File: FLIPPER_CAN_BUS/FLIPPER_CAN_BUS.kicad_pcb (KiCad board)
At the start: 2 copper layers, 62.8 x 21.2 mm, 25 parts, among them J1 Conn_01x02, J2 Conn_01x10_Socket, J3 Conn_01x08_Socket, U1 TJA1051T/3, U2 MCP2515-xST, U3 AP3602AKTR-G1, Y1 16 Mhz

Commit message: upd
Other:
- board text added: "+3V3"
- board text added: "5V"
- board text added: "CS"
- board text added: "GND"
- board text added: "INT"
- board text added: "MISO"
- board text added: "MOSI"
- board text added: "RST"
- board text added: "SCK"
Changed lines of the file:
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@@
     (property "manf#" "0603F104Z160CT")
     (attr smd)
-    (fp_text reference "C11" (at 2.130777 0.011726 -180) (layer "F.SilkS")
+    (fp_text reference "C11" (at -0.042823 -1.190674 -90) (layer "F.SilkS")
         (effects (font (size 0.5 0.5) (thickness 0.125)))
     )
@@
     (property "manf#" "0805YC106KAT2A")
     (attr smd)
-    (fp_text reference "C8" (at 2.133277 0.091726 -180) (layer "F.SilkS")
+    (fp_text reference "C8" (at 0.000477 1.110126 -90) (layer "F.SilkS")
         (effects (font (size 0.5 0.5) (thickness 0.125)))
     )
@@
   (gr_arc (start 143.8 71.6) (mid 145.497056 72.302944) (end 146.2 74)
     (stroke (width 0.1) (type default)) (layer "Edge.Cuts"))
-  (gr_text "CAN_BUS\n" (at 92.58 86.8) (layer "F.SilkS")
+  (gr_text "GND\n" (at 127.2032 88.9 90) (layer "F.SilkS")
+    (effects (font (size 0.7 0.7) (thickness 0.15)) (justify left bottom))
+  )
+  (gr_text "GND\n" (at 145.0848 88.9 90) (layer "F.SilkS")
+    (effects (font (size 0.7 0.7) (thickness 0.15)) (justify left bottom))
+  )
+  (gr_text "MISO" (at 91.6432 88.9 90) (layer "F.SilkS")
+    (effects (font (size 0.7 0.7) (thickness 0.15)) (justify left bottom))
+  )
+  (gr_text "CAN_BUS\n" (at 92.58 85.4456) (layer "F.SilkS")
     (effects (font (size 1 1) (thickness 0.25) bold) (justify left bottom))
   )
-  (gr_text "FLIPPER_SHIELD\n" (at 90.24 84.3) (layer "F.SilkS")
+  (gr_text "RST" (at 101.8032 88.9 90) (layer "F.SilkS")
+    (effects (font (size 0.7 0.7) (thickness 0.15)) (justify left bottom))
+  )
+  (gr_text "SCK" (at 96.7232 88.9 90) (layer "F.SilkS")
+    (effects (font (size 0.7 0.7) (thickness 0.15)) (justify left bottom))
+  )
+  (gr_text "FLIPPER_SHIELD\n" (at 90.24 83.6168) (layer "F.SilkS")
     (effects (font (size 1 1) (thickness 0.25) bold) (justify left bottom))
   )
+  (gr_text "5V\n" (at 86.36 88.9 90) (layer "F.SilkS")
+    (effects (font (size 0.7 0.7) (thickness 0.15)) (justify left bottom))
+  )
+  (gr_text "+3V3\n\n" (at 120.65 92.0496 90) (layer "F.SilkS")
+    (effects (font (size 0.7 0.7) (thickness 0.15)) (justify left bottom))
+  )
+  (gr_text "CS" (at 94.1324 88.9 90) (layer "F.SilkS")
+    (effects (font (size 0.7 0.7) (thickness 0.15)) (justify left bottom))
+  )
+  (gr_text "MOSI\n" (at 89.1032 88.8492 90) (layer "F.SilkS")
+    (effects (font (size 0.7 0.7) (thickness 0.15)) (justify left bottom))
+  )
+  (gr_text "GND" (at 106.3244 91.5924 90) (layer "F.SilkS")
+    (effects (font (size 0.7 0.7) (thickness 0.15)) (justify left bottom))
+  )
+  (gr_text "INT" (at 124.7648 88.9 90) (layer "F.SilkS")
+    (effects (font (size 0.7 0.7) (thickness 0.15)) (justify left bottom))
+  )
   (dimension (type aligned) (layer "Margin")

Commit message: upd
CSV
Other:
- board size 62.8 x 21.2 mm -> 62.8 x 23.2 mm
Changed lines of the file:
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@@
     (property "manf#" "PZ2.54-1*20-WZ")
     (attr through_hole)
-    (fp_text reference "J3" (at 4.385 2.27 90) (layer "B.SilkS")
+    (fp_text reference "J3" (at -1.964 -8.7736 -180) (layer "B.SilkS")
         (effects (font (size 0.5 0.5) (thickness 0.125)) (justify mirror))
     )
@@
     (property "manf#" "PZ2.54-1*20-WZ")
     (attr through_hole)
-    (fp_text reference "J2" (at 4.385 2.27 90) (layer "B.SilkS")
+    (fp_text reference "J2" (at -2.218 -12.482 -180) (layer "B.SilkS")
         (effects (font (size 0.5 0.5) (thickness 0.125)) (justify mirror))
     )
@@
   (gr_line (start 146.2 74) (end 146.2 90.4)
     (stroke (width 0.1) (type default)) (layer "Edge.Cuts"))
-  (gr_line (start 143.8 92.8) (end 86 92.8)
+  (gr_line (start 146.2 90.4) (end 146.2 92.6)
+    (stroke (width 0.1) (type default)) (layer "Edge.Cuts"))
+  (gr_arc (start 85.6 94.809943) (mid 84.037334 94.162666) (end 83.390057 92.6)
     (stroke (width 0.1) (type default)) (layer "Edge.Cuts"))
   (gr_line (start 86.2 71.592867) (end 143.8 71.592867)
     (stroke (width 0.1) (type default)) (layer "Edge.Cuts"))
-  (gr_arc (start 86 92.80768) (mid 84.156092 92.043908) (end 83.39232 90.2)
+  (gr_line (start 83.39232 90.2) (end 83.39232 92.6)
     (stroke (width 0.1) (type default)) (layer "Edge.Cuts"))
   (gr_line (start 83.39232 90.2) (end 83.39232 74.4)
     (stroke (width 0.1) (type default)) (layer "Edge.Cuts"))
-  (gr_arc (start 146.2 90.4) (mid 145.497056 92.097056) (end 143.8 92.8)
-    (stroke (width 0.1) (type default)) (layer "Edge.Cuts"))
   (gr_arc (start 83.392867 74.4) (mid 84.215057 72.415057) (end 86.2 71.592867)
+    (stroke (width 0.1) (type default)) (layer "Edge.Cuts"))
+  (gr_arc (start 146.2 92.6) (mid 145.555635 94.155635) (end 144 94.8)
+    (stroke (width 0.1) (type default)) (layer "Edge.Cuts"))
+  (gr_line (start 85.6 94.809943) (end 144 94.809943)
     (stroke (width 0.1) (type default)) (layer "Edge.Cuts"))
   (gr_arc (start 143.8 71.6) (mid 145.497056 72.302944) (end 146.2 74)
@@
   )
   (dimension (type aligned) (layer "Margin")
+    (pts (xy 85.6 94.809943) (xy 85.6 71.592867))
+    (height -5.082)
+    (gr_text "23.2171 mm" (at 79.368 83.201405 90) (layer "Margin")
+      (effects (font (size 1 1) (thickness 0.15)))
+    )
+    (format (prefix "") (suffix "") (units 3) (units_format 1) (precision 4))
+    (style (thickness 0.15) (arrow_length 1.27) (text_position_mode 0) (extension_height 0.58642) (extension_offset 0.5) keep_text_aligned)
+  )
+  (dimension (type aligned) (layer "Margin")
     (pts (xy 83.392867 74.4) (xy 146.2 74.4))
     (height -5.04)
     (gr_text "62.8071 mm" (at 114.796434 68.21) (layer "Margin")
-      (effects (font (size 1 1) (thickness 0.15)))
-    )
-    (format (prefix "") (suffix "") (units 3) (units_format 1) (precision 4))
-    (style (thickness 0.15) (arrow_length 1.27) (text_position_mode 0) (extension_height 0.58642) (extension_offset 0.5) keep_text_aligned)
-  )
-  (dimension (type aligned) (layer "Margin")
-    (pts (xy 86.2 71.592867) (xy 86.2 92.80768))
-    (height 4.289999)
-    (gr_text "21.2148 mm" (at 80.760001 82.200274 90) (layer "Margin")
       (effects (font (size 1 1) (thickness 0.15)))
     )
@@
       (pts
         (xy 83.38 71.59)
-        (xy 83.3937 92.797253)
-        (xy 146.224173 92.819707)
+        (xy 83.39491 94.669033)
+        (xy 146.225242 94.691486)
         (xy 146.212054 71.59)
       )

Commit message: upd
upd bom
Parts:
- added kibuzzard-644AD570: G***, kibuzzard-644AD570, F.Cu at (91.1, 87.8)
- added kibuzzard-644AD57B: G***, kibuzzard-644AD57B, F.Cu at (88.6, 87.8)
- added kibuzzard-644AD586: G***, kibuzzard-644AD586, F.Cu at (93.7, 88.2)
- added kibuzzard-644AD591: G***, kibuzzard-644AD591, F.Cu at (96.3, 88.0)
- added kibuzzard-644AD5B8: G***, kibuzzard-644AD5B8, F.Cu at (101.3, 88.0)
- added kibuzzard-644AD5D8: G***, kibuzzard-644AD5D8, F.Cu at (119.1, 90.6)
- added kibuzzard-644AD5FD: G***, kibuzzard-644AD5FD, F.Cu at (126.7, 88.0)
- added kibuzzard-644AD5FD: G***, kibuzzard-644AD5FD, F.Cu at (144.5, 88.0)
- added kibuzzard-644AD5FD: G***, kibuzzard-644AD5FD, F.Cu at (106.1, 90.6)
- added kibuzzard-644AD616: G***, kibuzzard-644AD616, F.Cu at (124.2, 88.0)
- D1: footprint PESD1CAN:SOT23-3 -> Package_TO_SOT_SMD:SOT-323_SC-70
- U1: footprint TJA1051T_3:SOT96-1 -> Package_SO:SOIC-8_3.9x4.9mm_P1.27mm
- U3: footprint footprints:SOT-23-6_DIO -> Package_TO_SOT_SMD:TSOT-23-6
- turned D1 to 180 degrees
- turned U1 to 0 degrees
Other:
- board text removed: "+3V3"
- board text removed: "5V"
- board text removed: "CS"
- board text removed: "GND"
- board text removed: "INT"
- board text removed: "MISO"
- board text removed: "MOSI"
- board text removed: "RST"
- board text removed: "SCK"

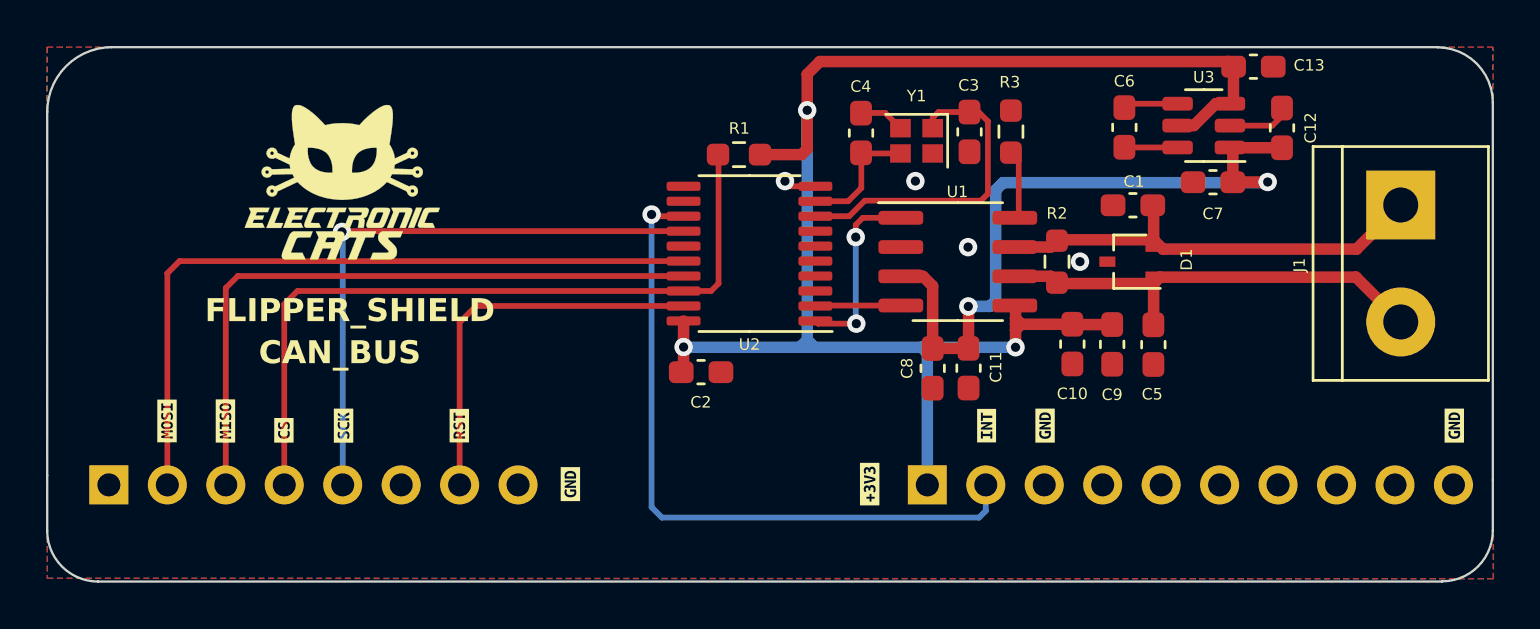
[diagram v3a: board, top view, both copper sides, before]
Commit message: Change_Capacitor_BOM
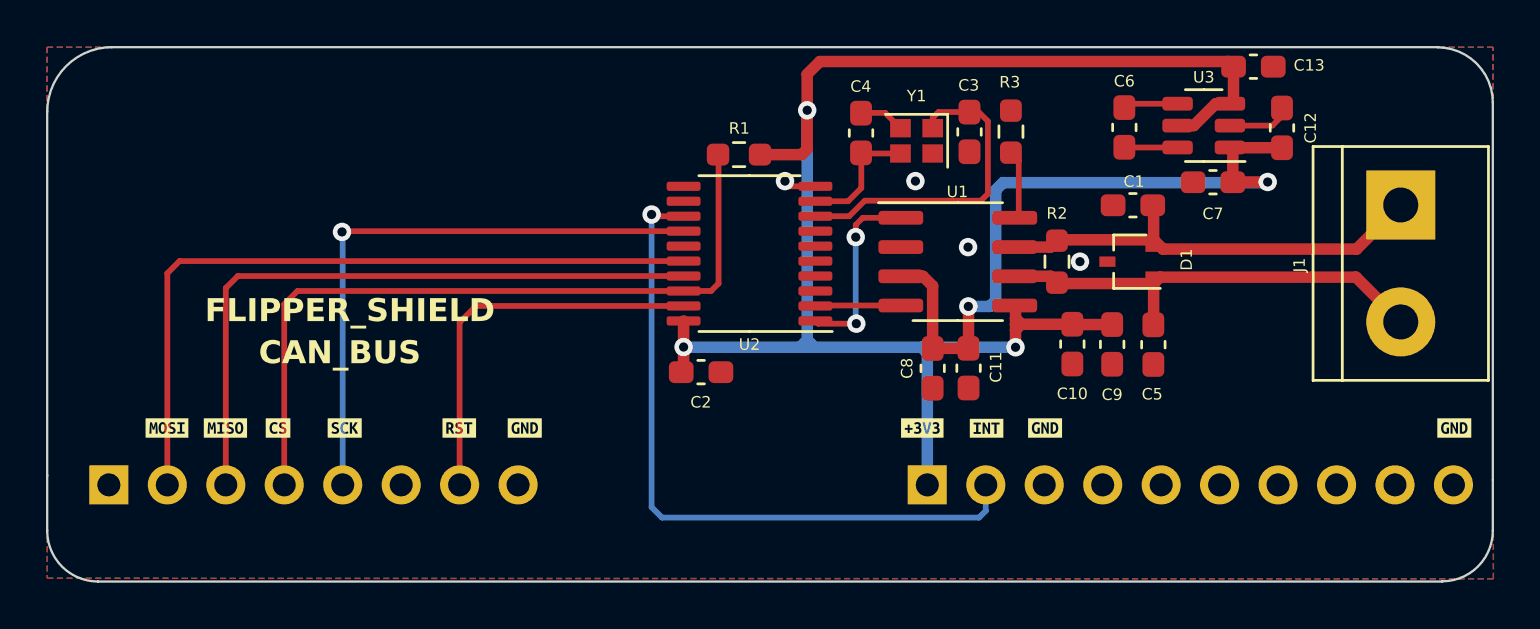
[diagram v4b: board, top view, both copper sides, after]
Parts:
- removed G***: LOGO, Logos:electronic_cats_logo_8x6
- moved kibuzzard-644AD5D8 3.34 mm to (121.4, 88.1), turned to 0 degrees
- moved kibuzzard-644AD5FD 3.14 mm to (104.1, 88.1), turned to 0 degrees
- moved kibuzzard-644AD570 0.30 mm to (91.1, 88.1), turned to 0 degrees
- moved kibuzzard-644AD57B 0.30 mm to (88.6, 88.1), turned to 0 degrees
- moved kibuzzard-644AD586 0.27 mm to (93.4, 88.1), turned to 0 degrees
- moved kibuzzard-644AD591 0.11 mm to (96.3, 88.1), turned to 0 degrees
- moved kibuzzard-644AD616 0.11 mm to (124.2, 88.1), turned to 0 degrees
- moved kibuzzard-644AD5B8 0.10 mm to (101.3, 88.1), turned to 0 degrees
- moved kibuzzard-644AD5FD 0.10 mm to (126.7, 88.1), turned to 0 degrees
- moved kibuzzard-644AD5FD 0.10 mm to (144.5, 88.1), turned to 0 degrees
